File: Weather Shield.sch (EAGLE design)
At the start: 46 parts, among them J1 GP-635T, Q1 BSS138, Q2 BSS138, U1 ARDUINO_R3_SHIELD, U2 3.3V MIC5219, U3 ALS-PT19, U4 MPL3115A2LGA8, U5 HTU21D

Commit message: Initial commit
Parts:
- removed C1: 1uF, SparkFun:CAP0603-CAP
- removed C13, C14: 10uF, SparkFun-Passives:CAP_POL1206
- removed C2: 0.1uF, SparkFun:CAP0603-CAP
- removed J1: GP-635T, SparkFun-Sensors:GP-635TSMD
- removed JP2: External Batt Bckup, SparkFun-Connectors:M02PTH
- removed R10: 10K, SparkFun-Passives:RESISTOR0603-RES
- removed R7: 1K, SparkFun:RESISTOR0603-RES
- removed R8: 3.9K, SparkFun:RESISTOR0603-RES
- removed R9: 4.7K, SparkFun:RESISTOR0603-RES
- removed S2: Serial Select, SparkFun-Electromechanical:SWITCH-DPDTAYZ0202
- removed U1: ARDUINO_R3_SHIELD, SparkFun-Boards:ARDUINO_R3_SHIELD
- removed U2: 3.3V MIC5219, SparkFun:V_REG_LDOSMD
- removed U3: ALS-PT19, SparkFun-Sensors:LIGHTSENSORALS
- D1: value Blue -> Red
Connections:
- removed net 3V_PWR_CTL: J1.PWRC, R9.2
- removed net BATT_LVL: R7.1, R8.2, U1.A2
- removed net GPS-RX: J1.RXA, S2.2
- removed net GPS-TX: J1.TXA, S2.5
- removed net GRXI: S2.6, U1.*D5
- removed net GTXO: S2.3, U1.D4
- removed net LIGHT: R10.2, U1.A1, U3.E1
- removed net PWR_CTL: R9.1, U1.*D6
- removed net RAW: C13.+, R8.1, U1.VIN, U2.EN, U2.IN
- removed net RXI: S2.4, U1.RX
- removed net TXO: S2.1, U1.TX
- removed net V_BATT: J1.VBATT, JP2.2
- net 3.3V: no longer C1.1, C14.+, C2.1, J1.VCC, U1.A3, U2.OUT, U3.C1
- net 5V: no longer U1.5V
- net GND: no longer C1.2, C13.-, C14.-, C2.2, J1.GND, JP2.1, R10.1, R7.2, U1.GND@0, U1.GND@1, U1.GND@2, U2.GND
- net HV_SCL: no longer U1.A5, U1.SCL
- net HV_SDA: no longer U1.A4, U1.SDA
- net RAIN: no longer U1.D2
- net STAT1: no longer U1.D7
- net STAT2: no longer U1.D8
- net WDIR: no longer U1.A0
- net WSPEED: no longer U1.*D3
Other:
- note added: "Rain sensor"
- note added: "Wind Speed & Direction"
- note removed: "1.5 to 3.5V"
- note removed: "Digital Pins 4 and 5 are used for software serial with switch is set to "Soft"."
- note removed: "External Batt Bckup"
- note removed: "GPS (optional)"
- note removed: "Light"
- note removed: "Max Current Output: 500mA"
- note removed: "Max Voltage Input: 16VDC"
- note removed: "Power"
- note removed: "Rain (optional)"
- note removed: "Wind (optional)"
- moved on the sheet: C5, C6, C7, C8, D1, D10, D3, D5, D6, D7, D8, D9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

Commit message: Initial commit
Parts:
- added PCB1: RASPBERRY_PI_B+_TPLACE, RASPBERRY_PI_Bplus:RASPBERRY_PI_B+_TPLACE
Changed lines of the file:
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@@
 <part name="LOGO1" library="SparkFun-Aesthetics" deviceset="OSHW-LOGO" device="M"/>
 <part name="FRAME1" library="frames" deviceset="DINA4_L" device=""/>
+<part name="PCB1" library="RASPBERRY_PI_Bplus" deviceset="RASPBERRY_PI_B+" device="_TPLACE"/>
 </parts>
 <sheets>
@@
 <instance part="FRAME1" gate="G$1" x="0" y="0"/>
 <instance part="FRAME1" gate="G$2" x="162.56" y="0"/>
+<instance part="PCB1" gate="G$1" x="137.16" y="91.44"/>
 </instances>
 <busses>
@@
 </schematic>
 </drawing>
+<compatibility>
+<note version="6.3" minversion="6.2.2" severity="warning">
+Since Version 6.2.2 text objects can contain more than one line,
+which will not be processed correctly with this version.
+</note>
+</compatibility>
 </eagle>

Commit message: FSE_Weather_Shield.lbr added
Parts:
- PCB1: value RASPBERRY_PI_B+_TPLACE -> RASPBERRY_PI_B+_DIM; device RASPBERRY_PI_Bplus:RASPBERRY_PI_B+_TPLACE -> FSE_Weather_Shield:RASPBERRY_PI_B+_DIM
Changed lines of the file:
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@@
 <part name="LOGO1" library="SparkFun-Aesthetics" deviceset="OSHW-LOGO" device="M"/>
 <part name="FRAME1" library="frames" deviceset="DINA4_L" device=""/>
-<part name="PCB1" library="RASPBERRY_PI_Bplus" deviceset="RASPBERRY_PI_B+" device="_TPLACE"/>
+<part name="PCB1" library="FSE_Weather_Shield" deviceset="RASPBERRY_PI_B+" device="_DIM"/>
 </parts>
 <sheets>
@@
 <instance part="FRAME1" gate="G$1" x="0" y="0"/>
 <instance part="FRAME1" gate="G$2" x="162.56" y="0"/>
-<instance part="PCB1" gate="G$1" x="137.16" y="91.44"/>
+<instance part="PCB1" gate="G$1" x="152.4" y="101.6"/>
 </instances>
 <busses>

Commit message: FSE_Weather_Shield.lbr added
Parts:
- added C1: 0.1uF, SparkFun:CAP0603-CAP
- added G1: 3V, battery:BATTERY-HOLDER_11.6MM
- added U1: DS3231SN, FSE_Weather_Shield:DS3231SN
- R1, R11, R12, R13, R14, R15, R16, R17, R2, R3, R4, R5, R6: device SparkFun:RESISTOR0603-RES -> rcl:R-EU_R0603
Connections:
- new net N$6: G1.+, U1.VBAT
- new net VCC: C1.1, U1.VCC
- net GND: now also C1.2, G1.-, U1.GND, U1.N.C., U1.N.C._2, U1.N.C._3, U1.N.C._4, U1.N.C._5, U1.N.C._6, U1.N.C._7, U1.N.C._8
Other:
- moved on the sheet: D1, D3, PCB1

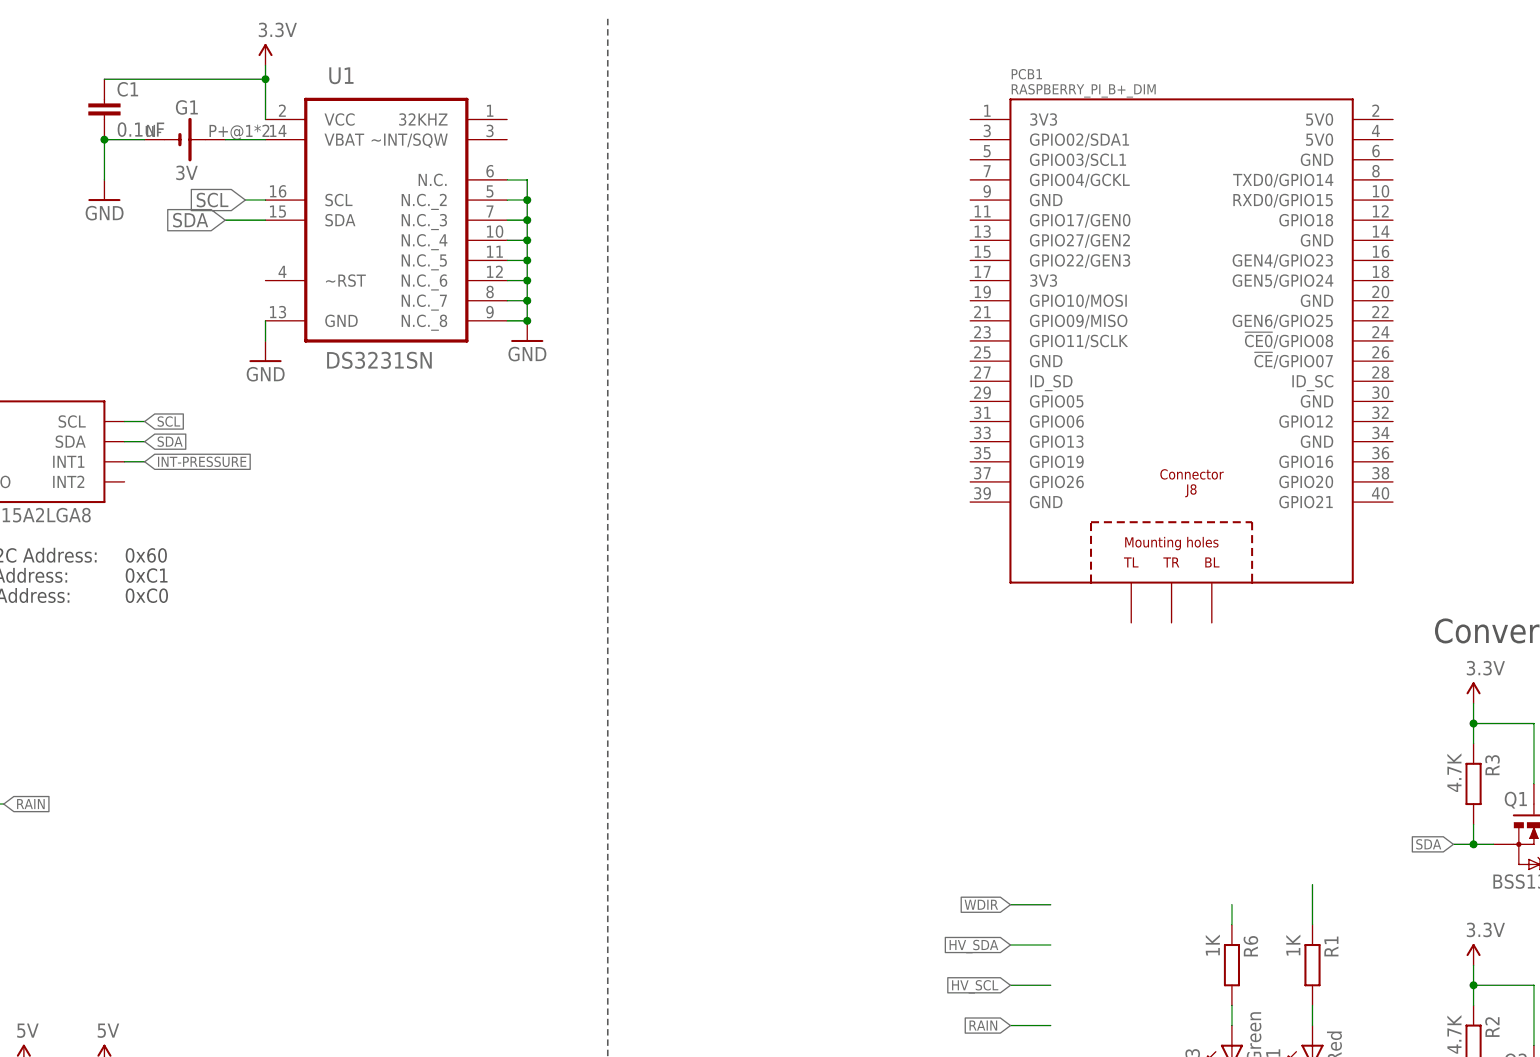
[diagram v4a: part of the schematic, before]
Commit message: FSE_Weather_Shield.lbr added
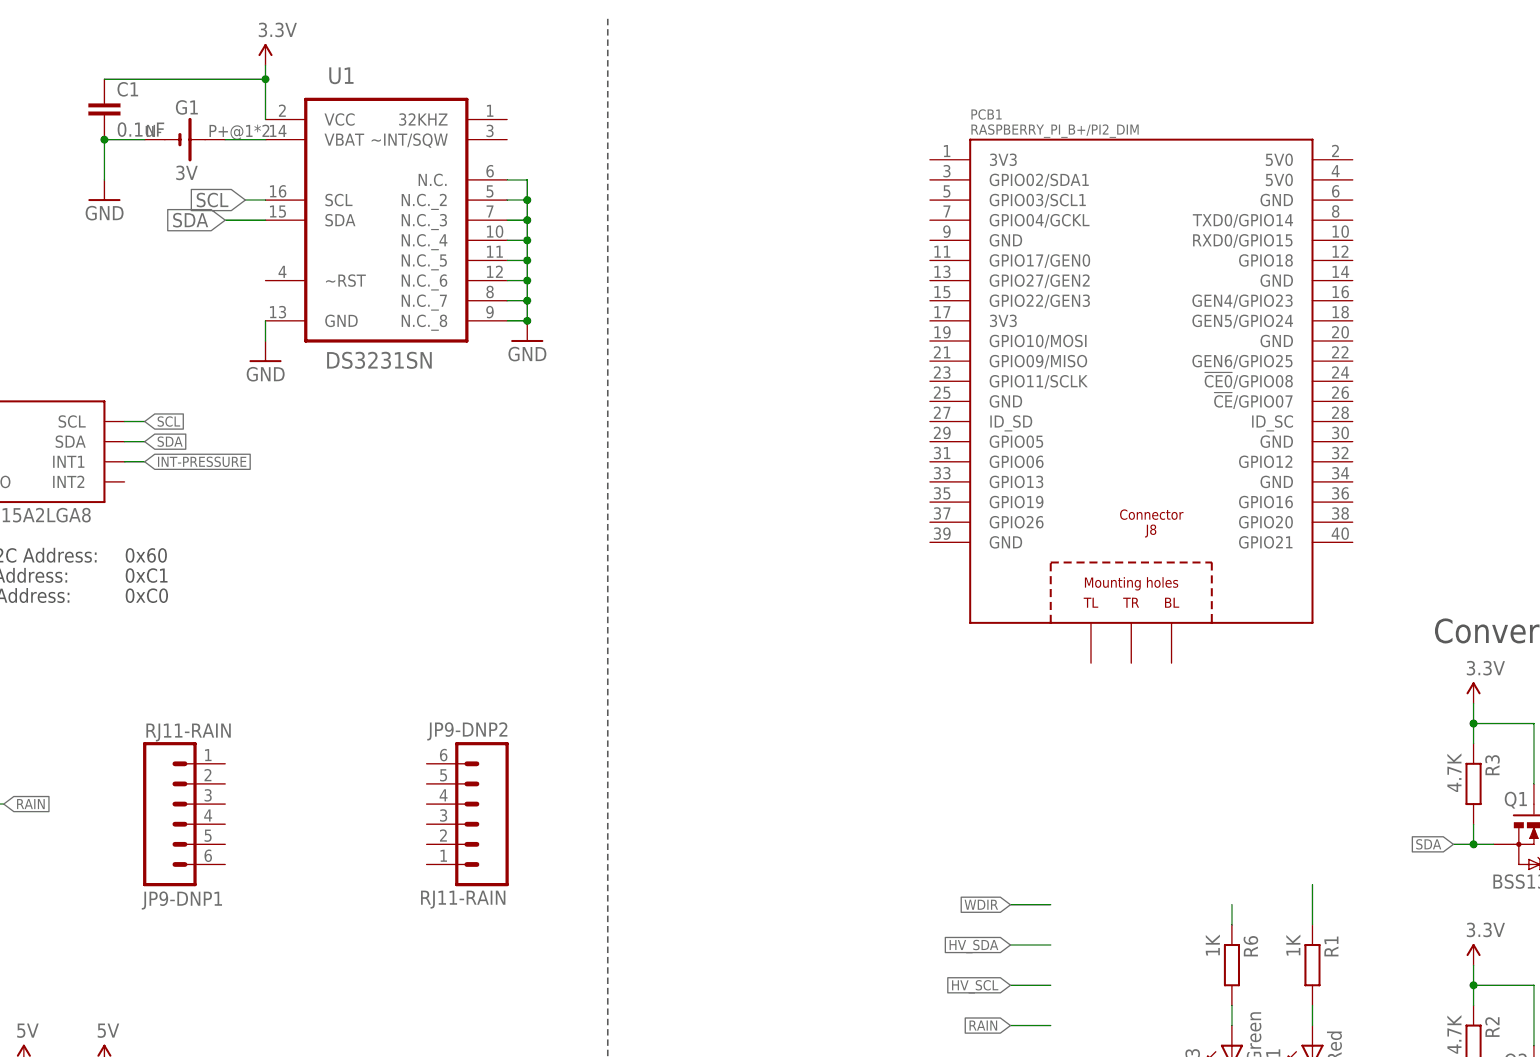
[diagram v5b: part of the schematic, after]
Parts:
- added JP9-DNP1, JP9-DNP2: RJ11-RAIN, SparkFun:RJ11-6PTH
- PCB1: value RASPBERRY_PI_B+_DIM -> RASPBERRY_PI_B+/PI2_DIM; device FSE_Weather_Shield:RASPBERRY_PI_B+_DIM -> FSE_Weather_Shield:RASPBERRY_PI_B+/PI2_DIM
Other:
- moved on the sheet: PCB1
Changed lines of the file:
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@@
 <layer number="54" name="bGND_GNDA" color="1" fill="9" visible="no" active="no"/>
 <layer number="56" name="wert" color="7" fill="1" visible="no" active="no"/>
+<layer number="90" name="Modules" color="5" fill="1" visible="yes" active="yes"/>
 <layer number="91" name="Nets" color="2" fill="1" visible="yes" active="yes"/>
 <layer number="92" name="Busses" color="1" fill="1" visible="yes" active="yes"/>
@@
 <part name="LOGO1" library="SparkFun-Aesthetics" deviceset="OSHW-LOGO" device="M"/>
 <part name="FRAME1" library="frames" deviceset="DINA4_L" device=""/>
-<part name="PCB1" library="FSE_Weather_Shield" deviceset="RASPBERRY_PI_B+" device="_DIM"/>
 <part name="U1" library="FSE_Weather_Shield" deviceset="DS3231SN" device=""/>
 <part name="GND1" library="SparkFun" deviceset="GND" device=""/>
@@
 <part name="GND5" library="SparkFun" deviceset="GND" device=""/>
 <part name="G1" library="battery" deviceset="BATTERY-HOLDER_11.6MM" device="" value="3V"/>
+<part name="PCB1" library="FSE_Weather_Shield" deviceset="RASPBERRY_PI_B+/PI2" device="_DIM"/>
+<part name="JP9-DNP1" library="SparkFun" deviceset="RJ11-6" device="PTH" value="RJ11-RAIN"/>
+<part name="JP9-DNP2" library="SparkFun" deviceset="RJ11-6" device="PTH" value="RJ11-RAIN"/>
 </parts>
 <sheets>
@@
 <instance part="FRAME1" gate="G$1" x="0" y="0"/>
 <instance part="FRAME1" gate="G$2" x="162.56" y="0"/>
-<instance part="PCB1" gate="G$1" x="200.66" y="144.78"/>
 <instance part="U1" gate="A" x="96.52" y="152.4"/>
 <instance part="GND1" gate="1" x="83.82" y="137.16" rot="MR0"/>
@@
 <instance part="GND5" gate="1" x="63.5" y="157.48" rot="MR0"/>
 <instance part="G1" gate="G$1" x="73.66" y="165.1"/>
+<instance part="PCB1" gate="G$1" x="195.58" y="139.7"/>
+<instance part="JP9-DNP1" gate="G$1" x="73.66" y="81.28" smashed="yes" rot="MR180">
+<attribute name="NAME" x="68.326" y="68.453" size="1.778" layer="95"/>
+<attribute name="VALUE" x="68.58" y="91.44" size="1.778" layer="96" rot="MR180"/>
+</instance>
+<instance part="JP9-DNP2" gate="G$1" x="109.22" y="78.74" smashed="yes" rot="MR0">
+<attribute name="NAME" x="114.554" y="91.567" size="1.778" layer="95" rot="R180"/>
+<attribute name="VALUE" x="114.3" y="68.58" size="1.778" layer="96" rot="MR0"/>
+</instance>
 </instances>
 <busses>

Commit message: initial project version
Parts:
- added D2: Blue, SparkFun:LED0603
- added R7: 1K, rcl:R-EU_R0603
- JP9-DNP1, JP9-DNP2: value RJ11-RAIN -> RJ11-6PTH
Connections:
- new net N$10: D2.A, R7.2
- new net STAT3: R7.1
- net GND: now also D2.C
- net SCL: now also U1.SCL
- net SDA: now also U1.SDA
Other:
- note added: "RTC Clock"
- note removed: "Conversion"
- note removed: "Sensors"
- moved on the sheet: C1, C5, C6, C7, C8, D10, D5, D6, D7, D8, D9, G1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

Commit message: initial project version
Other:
- moved on the sheet: PCB1
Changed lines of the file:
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@@
 <instance part="GND5" gate="1" x="7.62" y="68.58" rot="MR0"/>
 <instance part="G1" gate="G$1" x="17.78" y="76.2"/>
-<instance part="PCB1" gate="G$1" x="195.58" y="139.7"/>
+<instance part="PCB1" gate="G$1" x="198.12" y="132.08"/>
 <instance part="JP9-DNP1" gate="G$1" x="139.7" y="88.9" smashed="yes" rot="MR180">
 <attribute name="NAME" x="134.366" y="76.073" size="1.778" layer="95"/>

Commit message: initial project version
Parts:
- added C10, C11: 1.0uF, rcl:C-EUC0603
- added C2, C9: 10uF, rcl:C-EUC0603
- added C3, C4: 47uF, SparkFun-Capacitors:47UF-TANT
- added D11, D4: ZLLS500, SparkFun-DiscreteSemi:ZLLS500ZLLS500
- added J7, J8: M023.5MM, SparkFun-Connectors:M023.5MM
- added JP1: (no value), SparkFun-Passives:JUMPER-2SMD-NC
- added JP2: (no value), SparkFun-Passives:JUMPER-2SMD-NO
- added JP3: JUMPER-PTH-2-NC, SparkFun-Passives:JUMPER-PTH-2-NC
- added L1: 68uH, SparkFun-Passives:INDUCTOR68UH-1A
- added R10: 24k, rcl:R-EU_R0603
- added R20: 220k, rcl:R-EU_R0603
- added R21, R23: not fitted, rcl:R-EU_R0603
- added R22: 10k, pot:TRIM_EU-S64Y
- added R8: 0.2, rcl:R-EU_R0603
- added R9: 9.1k, rcl:R-EU_R0603
- added TP1: SET, testpad:PTR1B1,27
- added U$1, U$2, U$3: DEAN_CONNECTOR, FSE_Weather_Shield:DEAN_CONNECTOR
- added U2: LT3652, SparkFun-PowerIC:LT3652
- C1, C5, C6, C7, C8: device SparkFun:CAP0603-CAP -> rcl:C-EUC0603
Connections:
- removed net STAT1: R1.1
- removed net STAT2: R6.1
- new net !CHRG: D3.C, U2.!CHRG
- new net !FAULT: D1.C, U2.!FAULT
- new net BOOST: C10.1, D11.C, U2.BOOST
- new net FB: R10.1, R20.2, R9.2
- new net N$14: J7.2, J8.1, JP1.1, U$1.-, U$2.+
- new net N$15: R20.1, U2.VFB
- new net N$16: C3.+, C4.+, C9.1, D11.A, JP3.1, R10.2, R21.2, R23.2, R8.2, U2.BAT
- new net SENSE: L1.2, R21.1, R23.1, R8.1, U2.SENSE
- new net SET: R22.S, TP1.TP, U2.VIN_REG
- new net SFSASDF: J7.1, JP2.1, U$1.+
- new net SW: C10.2, D4.C, L1.1, U2.SW
- new net TIMER: C11.2, U2.TIMER
- new net VIN: C2.1, JP1.2, JP2.2, R22.E, U2.!SHDN, U2.VIN
- new net V_BATT: JP3.2, R1.1, R6.1, U$3.+
- net GND: now also C11.1, C2.2, C3.-, C4.-, C9.2, D4.A, J8.2, R22.A, R9.1, U$2.-, U$3.-, U2.GND_PAD; no longer D1.C, D3.C
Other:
- note added: "C=1uf -> t_EOC = 4.4h Connect to Ground if not needed"
- note added: "Cut the JP3 trace to measure output current. Adjust trim pot until output current reaches its maximum."
- note added: "Ichg = .1/(R8) Add more Resitors in parallel to increase Ichg"
- note added: "NB: With both JP1 and JP2 shorted, the second power input is also shorted! This may result in damage to your power source. You've been warned!"
- note added: "To add a second bank of solar cells, short JP2 and clear JP1."
- note added: "Voltage at SET can be used to set MPPT level. In full sun, adjust pot until V_SET = 2.8V."
- moved on the sheet: C1, C5, C6, C7, C8, D1, D10, D2, D3, D5, D6, D7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
